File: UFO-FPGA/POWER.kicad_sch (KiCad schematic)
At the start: 35 parts, among them J5 USB_B_Micro, Q1 2N7002, U6 PWR convert, U7 PWR convert

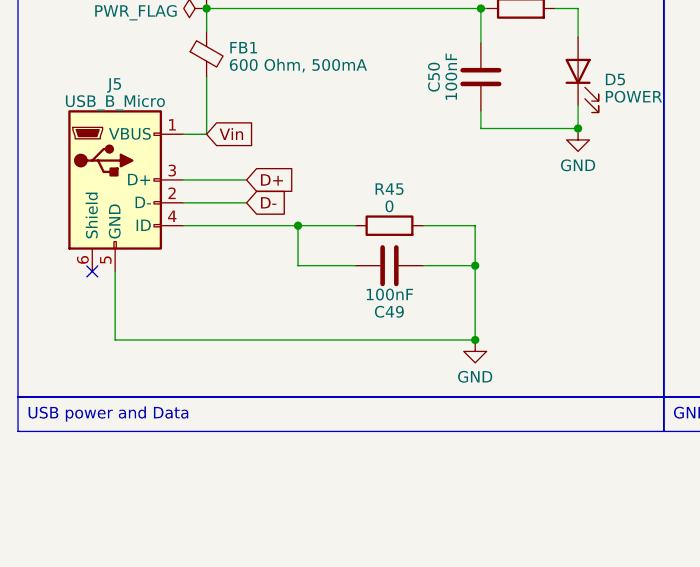
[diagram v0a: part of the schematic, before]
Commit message: pcb placement
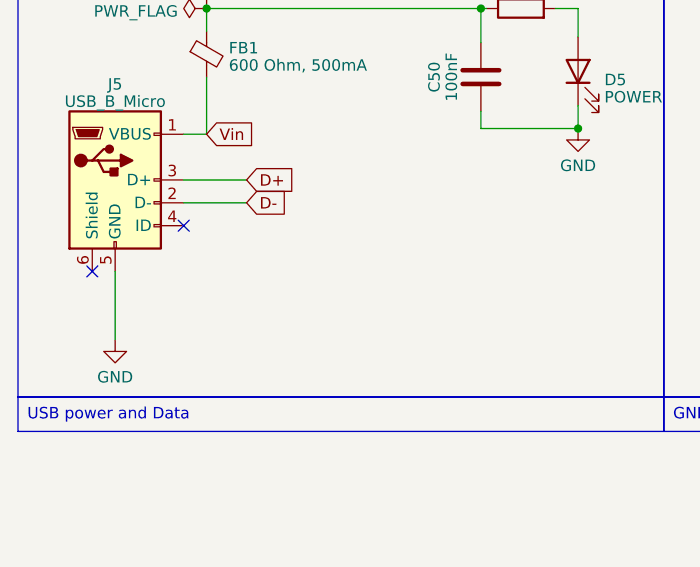
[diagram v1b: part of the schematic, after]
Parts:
- removed C49: 100nF, Capacitor_SMD:C_0805_2012Metric_Pad1.18x1.45mm_HandSolder, symbol Device:C
- removed R45: 0, Resistor_SMD:R_0805_2012Metric_Pad1.20x1.40mm_HandSolder, symbol Device:R
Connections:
- no-connect marks 10 -> 11
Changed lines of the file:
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@@
   (junction (at 86.36 102.235) (diameter 0) (color 0 0 0 0)
   )
-  (junction (at 55.245 113.03) (diameter 0) (color 0 0 0 0)
-  )
   (junction (at 169.545 100.33) (diameter 0) (color 0 0 0 0)
   )
@@
   (junction (at 187.96 100.33) (diameter 0) (color 0 0 0 0)
   )
-  (junction (at 74.93 125.73) (diameter 0) (color 0 0 0 0)
-  )
   (junction (at 179.07 86.36) (diameter 0) (color 0 0 0 0)
   )
@@
   (junction (at 160.655 100.33) (diameter 0) (color 0 0 0 0)
   )
-  (junction (at 74.93 117.475) (diameter 0) (color 0 0 0 0)
-  )
   (junction (at 117.475 109.855) (diameter 0) (color 0 0 0 0)
   )
@@
   (no_connect (at 32.385 118.11))
   (no_connect (at 86.995 43.18))
+  (no_connect (at 42.545 113.03))
   (no_connect (at 86.995 48.26))
   (no_connect (at 219.71 46.355))
@@
     (stroke (width 0) (type default))
   )
-  (wire (pts (xy 69.215 113.03) (xy 74.93 113.03))
-    (stroke (width 0) (type default))
-  )
   (wire (pts (xy 75.565 92.71) (xy 75.565 88.9))
     (stroke (width 0) (type default))
@@
     (stroke (width 0) (type default))
   )
-  (wire (pts (xy 55.245 117.475) (xy 55.245 113.03))
-    (stroke (width 0) (type default))
-  )
-  (wire (pts (xy 42.545 113.03) (xy 55.245 113.03))
-    (stroke (width 0) (type default))
-  )
   (wire (pts (xy 41.91 26.035) (xy 46.99 26.035))
     (stroke (width 0) (type default))
@@
     (stroke (width 0) (type default))
   )
-  (wire (pts (xy 69.215 117.475) (xy 74.93 117.475))
-    (stroke (width 0) (type default))
-  )
   (wire (pts (xy 160.655 86.36) (xy 169.545 86.36))
     (stroke (width 0) (type default))
   )
-  (wire (pts (xy 74.93 113.03) (xy 74.93 117.475))
-    (stroke (width 0) (type default))
-  )
   (wire (pts (xy 184.785 48.895) (xy 184.785 48.26))
     (stroke (width 0) (type default))
@@
     (stroke (width 0) (type default))
   )
-  (wire (pts (xy 74.93 117.475) (xy 74.93 125.73))
-    (stroke (width 0) (type default))
-  )
   (wire (pts (xy 160.655 86.36) (xy 160.655 89.535))
     (stroke (width 0) (type default))
@@
     (stroke (width 0) (type default))
   )
-  (wire (pts (xy 34.925 125.73) (xy 74.93 125.73))
-    (stroke (width 0) (type default))
-  )
   (wire (pts (xy 242.57 36.83) (xy 242.57 64.135))
     (stroke (width 0) (type default))
@@
     (stroke (width 0) (type default))
   )
-  (wire (pts (xy 61.595 117.475) (xy 55.245 117.475))
-    (stroke (width 0) (type default))
-  )
   (wire (pts (xy 83.82 88.9) (xy 86.36 88.9))
     (stroke (width 0) (type default))
@@
     (stroke (width 0) (type default))
   )
-  (wire (pts (xy 55.245 113.03) (xy 61.595 113.03))
-    (stroke (width 0) (type default))
-  )
   (wire (pts (xy 86.995 28.575) (xy 90.17 28.575))
     (stroke (width 0) (type default))
@@
     )
   )
-  (symbol (lib_id "Device:C") (at 65.405 117.475 90) (mirror x) (unit 1)
-    (in_bom yes) (on_board yes) (dnp no)
-    (property "Reference" "C49" (at 65.405 122.6439 90)
-      (effects (font (size 1.27 1.27)))
-    )
-    (property "Value" "100nF" (at 65.405 120.7229 90)
-      (effects (font (size 1.27 1.27)))
-    )
-    (property "Footprint" "Capacitor_SMD:C_0805_2012Metric_Pad1.18x1.45mm_HandSolder" (at 69.215 118.4402 0)
-      (effects (font (size 1.27 1.27)) hide)
-    )
-    (property "Datasheet" "~" (at 65.405 117.475 0)
-      (effects (font (size 1.27 1.27)) hide)
-    )
-    (pin "1")
-    (pin "2")
-    (instances
-      (project "POWER"
-        (path "/1a19c6f3-4fbd-4092-903c-8e5414c10419"
-          (reference "C49") (unit 1)
-        )
-      )
-      (project "UFO-FPGA"
-        (path "/b3168f6a-c732-41d3-aeeb-d97dd2f1bb65/abe08156-b909-4d2d-ad35-f723f4a728d5"
-          (reference "C39") (unit 1)
-        )
-      )
-    )
-  )
   (symbol (lib_id "power:GND") (at 46.99 35.56 0) (unit 1)
     (in_bom yes) (on_board yes) (dnp no) (fields_autoplaced)
@@
     )
   )
-  (symbol (lib_id "power:GND") (at 74.93 125.73 0) (unit 1)
+  (symbol (lib_id "power:GND") (at 34.925 125.73 0) (unit 1)
     (in_bom yes) (on_board yes) (dnp no) (fields_autoplaced)
-    (property "Reference" "#PWR063" (at 74.93 132.08 0)
+    (property "Reference" "#PWR063" (at 34.925 132.08 0)
       (effects (font (size 1.27 1.27)) hide)
     )
-    (property "Value" "GND" (at 74.93 129.8655 0)
+    (property "Value" "GND" (at 34.925 129.8655 0)
       (effects (font (size 1.27 1.27)))
     )
-    (property "Footprint" "" (at 74.93 125.73 0)
+    (property "Footprint" "" (at 34.925 125.73 0)
       (effects (font (size 1.27 1.27)) hide)
     )
-    (property "Datasheet" "" (at 74.93 125.73 0)
+    (property "Datasheet" "" (at 34.925 125.73 0)
       (effects (font (size 1.27 1.27)) hide)
     )
@@
       (project "UFO-FPGA"
         (path "/b3168f6a-c732-41d3-aeeb-d97dd2f1bb65/abe08156-b909-4d2d-ad35-f723f4a728d5"
-          (reference "POWER1") (unit 1)
+          (reference "PWR1") (unit 1)
         )
       )
@@
         )
       )
-    )
-  )
-  (symbol (lib_id "Device:R") (at 65.405 113.03 90) (unit 1)
-    (in_bom yes) (on_board yes) (dnp no) (fields_autoplaced)
-    (property "Reference" "R45" (at 65.405 109.0041 90)
-      (effects (font (size 1.27 1.27)))
-    )
-    (property "Value" "0" (at 65.405 110.9251 90)
-      (effects (font (size 1.27 1.27)))
-    )
-    (property "Footprint" "Resistor_SMD:R_0805_2012Metric_Pad1.20x1.40mm_HandSolder" (at 65.405 114.808 90)
-      (effects (font (size 1.27 1.27)) hide)
-    )
-    (property "Datasheet" "~" (at 65.405 113.03 0)
-      (effects (font (size 1.27 1.27)) hide)
-    )
-    (pin "1")
-    (pin "2")
-    (instances
-      (project "POWER"
-        (path "/1a19c6f3-4fbd-4092-903c-8e5414c10419"
-          (reference "R45") (unit 1)
-        )
-      )
-      (project "UFO-FPGA"
-        (path "/b3168f6a-c732-41d3-aeeb-d97dd2f1bb65/abe08156-b909-4d2d-ad35-f723f4a728d5"
-          (reference "R35") (unit 1)
-        )
-      )

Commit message: pcb 0603
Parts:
- C14, C3, C38, C39, C4, C42, C43, C50, C6: footprint Capacitor_SMD:C_0805_2012Metric_Pad1.18x1.45mm_HandSolder -> Capacitor_SMD:C_0603_1608Metric_Pad1.08x0.95mm_HandSolder
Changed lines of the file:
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@@
       (effects (font (size 1.27 1.27)) (justify left))
     )
-    (property "Footprint" "Capacitor_SMD:C_0805_2012Metric_Pad1.18x1.45mm_HandSolder" (at 180.0352 97.155 0)
+    (property "Footprint" "Capacitor_SMD:C_0603_1608Metric_Pad1.08x0.95mm_HandSolder" (at 180.0352 97.155 0)
       (effects (font (size 1.27 1.27)) hide)
     )
@@
       (effects (font (size 1.27 1.27)) (justify left))
     )
-    (property "Footprint" "Capacitor_SMD:C_0805_2012Metric_Pad1.18x1.45mm_HandSolder" (at 234.6452 36.83 0)
+    (property "Footprint" "Capacitor_SMD:C_0603_1608Metric_Pad1.08x0.95mm_HandSolder" (at 234.6452 36.83 0)
       (effects (font (size 1.27 1.27)) hide)
     )
@@
       (effects (font (size 1.27 1.27)) (justify left))
     )
-    (property "Footprint" "Capacitor_SMD:C_0805_2012Metric_Pad1.18x1.45mm_HandSolder" (at 53.0352 55.88 0)
+    (property "Footprint" "Capacitor_SMD:C_0603_1608Metric_Pad1.08x0.95mm_HandSolder" (at 53.0352 55.88 0)
       (effects (font (size 1.27 1.27)) hide)
     )
@@
       (effects (font (size 1.27 1.27)) (justify left))
     )
-    (property "Footprint" "Capacitor_SMD:C_0805_2012Metric_Pad1.18x1.45mm_HandSolder" (at 181.9402 117.475 0)
+    (property "Footprint" "Capacitor_SMD:C_0603_1608Metric_Pad1.08x0.95mm_HandSolder" (at 181.9402 117.475 0)
       (effects (font (size 1.27 1.27)) hide)
     )
@@
       (effects (font (size 1.27 1.27)))
     )
-    (property "Footprint" "Capacitor_SMD:C_0805_2012Metric_Pad1.18x1.45mm_HandSolder" (at 74.5998 100.33 0)
+    (property "Footprint" "Capacitor_SMD:C_0603_1608Metric_Pad1.08x0.95mm_HandSolder" (at 74.5998 100.33 0)
       (effects (font (size 1.27 1.27)) hide)
     )
@@
       (effects (font (size 1.27 1.27)) (justify left))
     )
-    (property "Footprint" "Capacitor_SMD:C_0805_2012Metric_Pad1.18x1.45mm_HandSolder" (at 105.7402 36.195 0)
+    (property "Footprint" "Capacitor_SMD:C_0603_1608Metric_Pad1.08x0.95mm_HandSolder" (at 105.7402 36.195 0)
       (effects (font (size 1.27 1.27)) hide)
     )
@@
       (effects (font (size 1.27 1.27)) (justify left))
     )
-    (property "Footprint" "Capacitor_SMD:C_0805_2012Metric_Pad1.18x1.45mm_HandSolder" (at 170.5102 97.155 0)
+    (property "Footprint" "Capacitor_SMD:C_0603_1608Metric_Pad1.08x0.95mm_HandSolder" (at 170.5102 97.155 0)
       (effects (font (size 1.27 1.27)) hide)
     )
@@
       (effects (font (size 1.27 1.27)) (justify left))
     )
-    (property "Footprint" "Capacitor_SMD:C_0805_2012Metric_Pad1.18x1.45mm_HandSolder" (at 188.9252 97.155 0)
+    (property "Footprint" "Capacitor_SMD:C_0603_1608Metric_Pad1.08x0.95mm_HandSolder" (at 188.9252 97.155 0)
       (effects (font (size 1.27 1.27)) hide)
     )
@@
       (effects (font (size 1.27 1.27)) (justify left))
     )
-    (property "Footprint" "Capacitor_SMD:C_0805_2012Metric_Pad1.18x1.45mm_HandSolder" (at 172.4152 117.475 0)
+    (property "Footprint" "Capacitor_SMD:C_0603_1608Metric_Pad1.08x0.95mm_HandSolder" (at 172.4152 117.475 0)
       (effects (font (size 1.27 1.27)) hide)
     )
@@
       (effects (font (size 1.27 1.27)) (justify left))
     )
-    (property "Footprint" "Capacitor_SMD:C_0805_2012Metric_Pad1.18x1.45mm_HandSolder" (at 161.6202 97.155 0)
+    (property "Footprint" "Capacitor_SMD:C_0603_1608Metric_Pad1.08x0.95mm_HandSolder" (at 161.6202 97.155 0)
       (effects (font (size 1.27 1.27)) hide)
     )
@@
       (effects (font (size 1.27 1.27)) (justify left))
     )
-    (property "Footprint" "Capacitor_SMD:C_0805_2012Metric_Pad1.18x1.45mm_HandSolder" (at 185.7502 56.515 0)
+    (property "Footprint" "Capacitor_SMD:C_0603_1608Metric_Pad1.08x0.95mm_HandSolder" (at 185.7502 56.515 0)
       (effects (font (size 1.27 1.27)) hide)
     )
@@
       (effects (font (size 1.27 1.27)) (justify left))
     )
-    (property "Footprint" "Capacitor_SMD:C_0805_2012Metric_Pad1.18x1.45mm_HandSolder" (at 162.8902 117.475 0)
-      (effects (font (size 1.27 1.27)) hide)
-    )
+    (property "Footprint" "Capacitor_SMD:C_0603_1608Metric_Pad1.08x0.95mm_HandSolder" (at 162.8902 117.475 0)
+      (effects (font (size 1.27 1.27)) hide)
+    )

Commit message: pcb
added John zendong
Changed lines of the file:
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@@
-    (effects (font (size 1.27 1.27)) (justify left bottom))
-  )
-  (label "+3v3" (at 242.57 29.21 0) (fields_autoplaced)
     (effects (font (size 1.27 1.27)) (justify left bottom))
   )

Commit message: pcb
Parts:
- C14, C4, C6: footprint Capacitor_SMD:C_0603_1608Metric_Pad1.08x0.95mm_HandSolder -> Capacitor_SMD:C_0805_2012Metric_Pad1.18x1.45mm_HandSolder
- TP1: footprint TestPoint:TestPoint_Pad_1.5x1.5mm -> TestPoint:TestPoint_Pad_1.0x1.0mm
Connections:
- net +1V2: no longer C14.1, C14.1, C2.1, C3.1
- net +3V3: now also C14.1, C14.1, C2.1, C3.1
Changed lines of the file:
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@@
   (junction (at 151.765 86.36) (diameter 0) (color 0 0 0 0)
   )
-  (junction (at 153.035 106.68) (diameter 0) (color 0 0 0 0)
-  )
   (junction (at 184.785 26.67) (diameter 0) (color 0 0 0 0)
   )
@@
   (junction (at 55.245 26.035) (diameter 0) (color 0 0 0 0)
   )
+  (junction (at 153.035 106.68) (diameter 0) (color 0 0 0 0)
+  )
   (no_connect (at 86.995 53.34))
   (no_connect (at 86.995 50.8))
@@
     )
   )
-  (symbol (lib_id "power:+1V2") (at 153.035 106.68 0) (unit 1)
-    (in_bom yes) (on_board yes) (dnp no) (fields_autoplaced)
-    (property "Reference" "#PWR067" (at 153.035 110.49 0)
-      (effects (font (size 1.27 1.27)) hide)
-    )
-    (property "Value" "+1V2" (at 153.035 103.1781 0)
-      (effects (font (size 1.27 1.27)))
-    )
-    (property "Footprint" "" (at 153.035 106.68 0)
-      (effects (font (size 1.27 1.27)) hide)
-    )
-    (property "Datasheet" "" (at 153.035 106.68 0)
-      (effects (font (size 1.27 1.27)) hide)
-    )
-    (pin "1")
-    (instances
-      (project "POWER"
-        (path "/1a19c6f3-4fbd-4092-903c-8e5414c10419"
-          (reference "#PWR067") (unit 1)
-        )
-      )
-      (project "UFO-FPGA"
-        (path "/b3168f6a-c732-41d3-aeeb-d97dd2f1bb65/abe08156-b909-4d2d-ad35-f723f4a728d5"
-          (reference "#PWR047") (unit 1)
-        )
-      )
-    )
-  )
   (symbol (lib_id "power:GND") (at 71.755 62.865 0) (unit 1)
     (in_bom yes) (on_board yes) (dnp no) (fields_autoplaced)
@@
       (effects (font (size 1.27 1.27)) (justify left))
     )
-    (property "Footprint" "Capacitor_SMD:C_0603_1608Metric_Pad1.08x0.95mm_HandSolder" (at 180.0352 97.155 0)
+    (property "Footprint" "Capacitor_SMD:C_0805_2012Metric_Pad1.18x1.45mm_HandSolder" (at 180.0352 97.155 0)
       (effects (font (size 1.27 1.27)) hide)
     )
@@
       (effects (font (size 1.27 1.27)) (justify right))
     )
-    (property "Footprint" "TestPoint:TestPoint_Pad_1.5x1.5mm" (at 229.87 91.44 0)
+    (property "Footprint" "TestPoint:TestPoint_Pad_1.0x1.0mm" (at 229.87 91.44 0)
       (effects (font (size 1.27 1.27)) hide)
     )
@@
       (effects (font (size 1.27 1.27)) (justify right))
     )
-    (property "Footprint" "TestPoint:TestPoint_Pad_1.5x1.5mm" (at 252.73 91.44 0)
+    (property "Footprint" "TestPoint:TestPoint_Pad_1.0x1.0mm" (at 252.73 91.44 0)
       (effects (font (size 1.27 1.27)) hide)
     )
@@
     )
   )
+  (symbol (lib_id "power:+3V3") (at 153.035 106.68 0) (unit 1)
+    (in_bom yes) (on_board yes) (dnp no) (fields_autoplaced)
+    (property "Reference" "#PWR047" (at 153.035 110.49 0)
+      (effects (font (size 1.27 1.27)) hide)
+    )
+    (property "Value" "+3V3" (at 153.035 103.1781 0)
+      (effects (font (size 1.27 1.27)))
+    )
+    (property "Footprint" "" (at 153.035 106.68 0)
+      (effects (font (size 1.27 1.27)) hide)
+    )
+    (property "Datasheet" "" (at 153.035 106.68 0)
+      (effects (font (size 1.27 1.27)) hide)
+    )
+    (pin "1")
+    (instances
+      (project "UFO-FPGA"
+        (path "/b3168f6a-c732-41d3-aeeb-d97dd2f1bb65/abe08156-b909-4d2d-ad35-f723f4a728d5"
+          (reference "#PWR047") (unit 1)
+        )
+      )
+    )
+  )
   (symbol (lib_id "power:+5V") (at 41.91 26.035 0) (unit 1)
     (in_bom yes) (on_board yes) (dnp no) (fields_autoplaced)
@@
       (effects (font (size 1.27 1.27)) (justify right))
     )
-    (property "Footprint" "TestPoint:TestPoint_Pad_1.5x1.5mm" (at 219.71 91.44 0)
+    (property "Footprint" "TestPoint:TestPoint_Pad_1.0x1.0mm" (at 219.71 91.44 0)
       (effects (font (size 1.27 1.27)) hide)
     )
@@
       (effects (font (size 1.27 1.27)) (justify left))
     )
-    (property "Footprint" "Capacitor_SMD:C_0603_1608Metric_Pad1.08x0.95mm_HandSolder" (at 170.5102 97.155 0)
+    (property "Footprint" "Capacitor_SMD:C_0805_2012Metric_Pad1.18x1.45mm_HandSolder" (at 170.5102 97.155 0)
       (effects (font (size 1.27 1.27)) hide)
     )
@@
       (effects (font (size 1.27 1.27)) (justify left))
     )
-    (property "Footprint" "Capacitor_SMD:C_0603_1608Metric_Pad1.08x0.95mm_HandSolder" (at 188.9252 97.155 0)
+    (property "Footprint" "Capacitor_SMD:C_0805_2012Metric_Pad1.18x1.45mm_HandSolder" (at 188.9252 97.155 0)
       (effects (font (size 1.27 1.27)) hide)
     )

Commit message: pcb
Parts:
- removed C37, C40, C41, C44: 47uF, Capacitor_SMD:C_1206_3216Metric_Pad1.33x1.80mm_HandSolder, symbol Device:C
- removed C38, C39, C42, C43: 10nF, Capacitor_SMD:C_0603_1608Metric_Pad1.08x0.95mm_HandSolder, symbol Device:C
- removed R35: 100k, Resistor_SMD:R_0805_2012Metric_Pad1.20x1.40mm_HandSolder, symbol Device:R
- removed R40: 100k, Resistor_SMD:R_0805_2012Metric, symbol Device:R
- removed R48: 1M, Resistor_SMD:R_0805_2012Metric_Pad1.20x1.40mm_HandSolder, symbol Device:R
- removed U6, U7: PWR convert, UFO-Footpints:W-QFN3535-20, symbol UFO_PARTS:AP7179D-13
- added C14, C5: 1uF, Capacitor_SMD:C_0805_2012Metric_Pad1.18x1.45mm_HandSolder, symbol Device:C
- added C25, C6: 10uF, Capacitor_SMD:C_0805_2012Metric_Pad1.18x1.45mm_HandSolder, symbol Device:C
- added R29: 1M, Resistor_SMD:R_0805_2012Metric_Pad1.20x1.40mm_HandSolder, symbol Device:R
- added U1: NCP187AMT120TAG (+1V2), Package_DFN_QFN:DFN-6-1EP_2x2mm_P0.65mm_EP1x1.6mm, symbol UFO_PARTS:NCP187AMT120TAG (+1V2)
- added U6: NCP187AMT330TAG (+3V3), Package_DFN_QFN:DFN-6-1EP_2x2mm_P0.65mm_EP1x1.6mm, symbol UFO_PARTS:NCP187AMT330TAG (+3V3)
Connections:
- net +1V2: now also C6.1, U1.5 (SNS), U1.6 (OUT)
- net +3V3: now also C25.1, U6.5 (SNS), U6.6 (OUT)
- net +5V: now also C14.1, C5.1, R29.2, U1.1 (IN), U6.1 (IN)
- net 3v3-EN: now also U6.2 (EN)
- net GND: now also C14.2, C25.2, C5.2, C6.2, U1.3 (GND), U6.3 (GND)
- net PG1V2: now also U1.4 (PG)
- new net: R29.1, U1.2 (EN)
- new net PG3v3: U6.4 (PG)
- no-connect marks 11 -> 2

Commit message: pcb
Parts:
- removed R48: 1M, Resistor_SMD:R_0805_2012Metric_Pad1.20x1.40mm_HandSolder, symbol Device:R
- added D5: POWER, LED_SMD:LED_0805_2012Metric_Pad1.15x1.40mm_HandSolder, symbol Device:LED
- added R46: 1K, Resistor_SMD:R_0805_2012Metric_Pad1.20x1.40mm_HandSolder, symbol Device:R
- added R47 (x2): 10k, Resistor_SMD:R_0805_2012Metric_Pad1.20x1.40mm_HandSolder, symbol Device:R
- R29: value 1M -> 0R
- R47: value 1M -> 10k
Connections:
- net +3V3: now also R46.1
- net +5V: now also R47.2
- net 3v3-EN: now also R47.1; no longer Q1.3 (D)
- net PG1V2: now also R47.2; no longer Q1.1 (G)
- net PG3v3: now also Q1.1 (G), R47.1
- new net: D5.1 (K), Q1.3 (D)
- new net: D5.2 (A), R46.2
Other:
- moved on the sheet: Q1, R47

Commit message: PCB
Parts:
- R46: value 1K -> 330R
- R47: value 10k -> 0
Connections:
- net GND: now also U1.7 (GND), U6.7 (GND)
- net LED-ON: now reaches D5.1 (K), Q1.3 (D)
- net RIND-ON: now reaches D5.2 (A), R46.2
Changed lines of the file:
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@@
     (stroke (width 0) (type default))
   )
-  (wire (pts (xy 101.6 45.72) (xy 97.155 45.72))
+  (wire (pts (xy 101.346 45.72) (xy 97.155 45.72))
     (stroke (width 0) (type default))
   )
@@
     (stroke (width 0) (type default))
   )
-  (wire (pts (xy 88.9 40.005) (xy 101.6 40.005))
+  (wire (pts (xy 88.9 40.005) (xy 101.346 40.005))
     (stroke (width 0) (type default))
   )
@@
     (stroke (width 0) (type default))
   )
-  (wire (pts (xy 120.015 40.005) (xy 123.19 40.005))
+  (wire (pts (xy 119.761 40.005) (xy 123.19 40.005))
     (stroke (width 0) (type default))
   )
@@
     (stroke (width 0) (type default))
   )
-  (wire (pts (xy 120.015 45.72) (xy 123.19 45.72))
+  (wire (pts (xy 119.761 45.72) (xy 123.19 45.72))
     (stroke (width 0) (type default))
   )
@@
     (stroke (width 0) (type default))
   )
-  (wire (pts (xy 120.015 42.545) (xy 123.19 42.545))
+  (wire (pts (xy 119.761 42.545) (xy 123.19 42.545))
     (stroke (width 0) (type default))
   )
@@
     (stroke (width 0) (type default))
   )
-  (wire (pts (xy 97.79 42.545) (xy 101.6 42.545))
+  (wire (pts (xy 97.79 42.545) (xy 101.346 42.545))
     (stroke (width 0) (type default))
   )
@@
     (effects (font (size 1.27 1.27)) (justify right bottom))
   )
+  (label "LED-ON" (at 137.668 104.902 0) (fields_autoplaced)
+    (effects (font (size 1.27 1.27)) (justify left bottom))
+  )
+  (label "RIND-ON" (at 137.668 95.758 0) (fields_autoplaced)
+    (effects (font (size 1.27 1.27)) (justify left bottom))
+  )
   (label "PG3v3" (at 200.025 46.355 0) (fields_autoplaced)
     (effects (font (size 1.27 1.27)) (justify left bottom))
@@
     (pin "5")
     (pin "6")
+    (pin "7")
     (instances
       (project "UFO-FPGA"
@@
       (effects (font (size 1.27 1.27)) (justify right))
     )
-    (property "Value" "10k" (at 112.903 114.9423 0)
+    (property "Value" "0" (at 112.903 114.9423 0)
       (effects (font (size 1.27 1.27)) (justify right))
     )
@@
       (effects (font (size 1.27 1.27)) (justify left))
     )
-    (property "Value" "1K" (at 139.446 91.4473 0)
+    (property "Value" "330R" (at 139.446 91.4473 0)
       (effects (font (size 1.27 1.27)) (justify left))
     )
@@
     )
   )
-  (symbol (lib_id "UFO_PARTS:NCP187AMT120TAG (+1V2)") (at 111.125 36.83 0) (unit 1)
+  (symbol (lib_id "UFO_PARTS:NCP187AMT120TAG (+1V2)") (at 110.871 36.83 0) (unit 1)
     (in_bom yes) (on_board yes) (dnp no) (fields_autoplaced)
-    (property "Reference" "U1" (at 110.8075 35.2171 0)
+    (property "Reference" "U1" (at 110.5535 35.2171 0)
       (effects (font (size 1.27 1.27)))
     )
-    (property "Value" "NCP187AMT120TAG (+1V2)" (at 110.8075 37.1381 0)
+    (property "Value" "NCP187AMT120TAG (+1V2)" (at 110.5535 37.1381 0)
       (effects (font (size 1.27 1.27)))
     )
-    (property "Footprint" "Package_DFN_QFN:DFN-6-1EP_2x2mm_P0.65mm_EP1x1.6mm" (at 111.76 33.655 0)
+    (property "Footprint" "Package_DFN_QFN:DFN-6-1EP_2x2mm_P0.65mm_EP1x1.6mm" (at 111.506 33.655 0)
       (effects (font (size 1.27 1.27)) hide)
     )
-    (property "Datasheet" "" (at 111.125 36.83 0)
+    (property "Datasheet" "" (at 110.871 36.83 0)
       (effects (font (size 1.27 1.27)) hide)
     )
@@
     (pin "5")
     (pin "6")
+    (pin "7")
     (instances
       (project "UFO-FPGA"
